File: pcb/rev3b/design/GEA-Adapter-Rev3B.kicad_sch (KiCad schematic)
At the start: 100 parts, among them J1 8P8C, J2 RECOVERY, J3 TC2030, Q3 CJ3407, Q4 CJ3407, Q5 MMBT3904, U10 TPS22810DBVR, U2 XIAO ESP32-C3 v1.3 (22-pad), U4 74LVC2G07, U5 74LVC2G07_3v3, U8 AP63205WU, U9 TPS22810DBVR

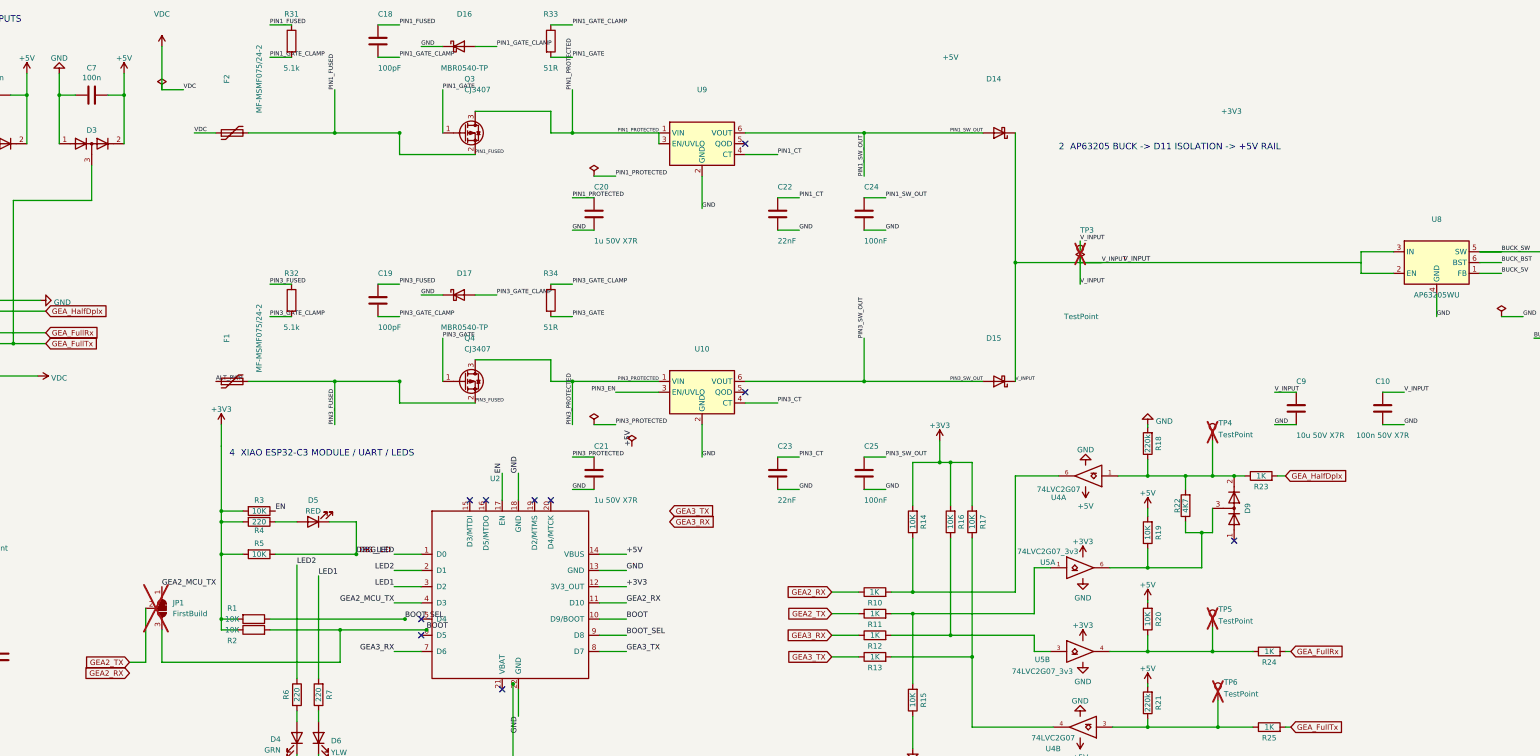
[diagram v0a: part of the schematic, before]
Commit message: fix(pcb): resolve Rev3B schematic warnings and label spacing
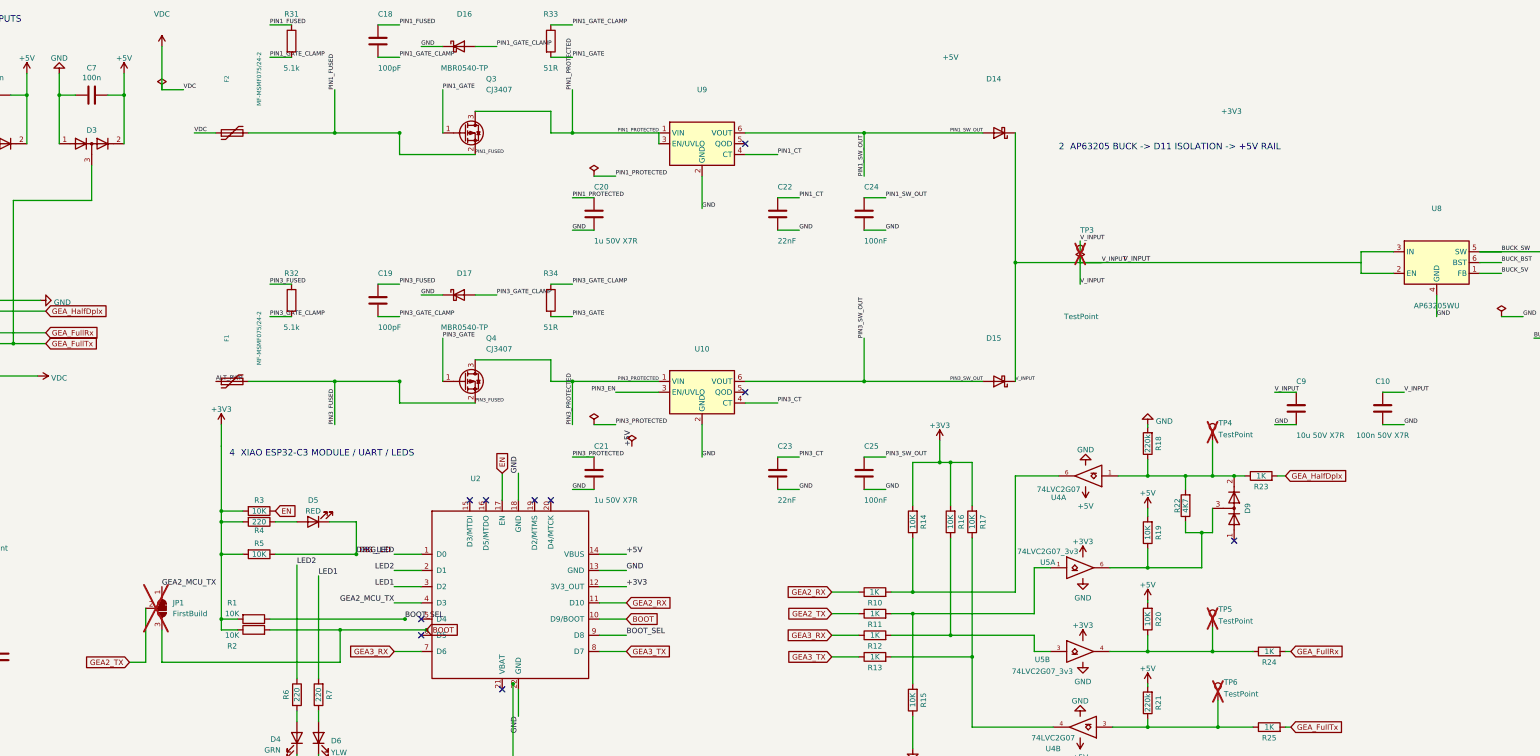
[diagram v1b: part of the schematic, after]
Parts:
- U4: symbol 74xGxx:74LVC2G07 -> GEA_Rev3B:74LVC2G07
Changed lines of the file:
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@@
 		)
 	)
-	(global_label "GEA3_TX"
-		(shape input)
-		(at 223.52 134.62 0)
-		(fields_autoplaced yes)
-		(effects
-			(font
-				(size 1.27 1.27)
-			)
-			(justify left)
-		)
-		(property "Intersheetrefs" "${INTERSHEET_REFS}"
-			(at 233.7128 134.62 0)
-			(effects
-				(font
-					(size 1.27 1.27)
-				)
-				(justify left)
-				(hide yes)
-			)
-		)
-	)
 	(global_label "GEA3_RX"
 		(shape input)
@@
 		)
 	)
-	(global_label "GEA3_RX"
-		(shape input)
-		(at 223.52 137.16 0)
-		(fields_autoplaced yes)
-		(effects
-			(font
-				(size 1.27 1.27)
-			)
-			(justify left)
-		)
-		(property "Intersheetrefs" "${INTERSHEET_REFS}"
-			(at 234.0152 137.16 0)
-			(effects
-				(font
-					(size 1.27 1.27)
-				)
-				(justify left)
-				(hide yes)
-			)
-		)
-	)
-	(global_label "GEA2_RX"
-		(shape input)
-		(at 96.52 172.72 180)
-		(fields_autoplaced yes)
-		(effects
-			(font
-				(size 1.27 1.27)
-			)
-			(justify right)
-		)
-		(property "Intersheetrefs" "${INTERSHEET_REFS}"
-			(at 86.0248 172.72 0)
-			(effects
-				(font
-					(size 1.27 1.27)
-				)
-				(justify right)
-				(hide yes)
-			)
-		)
-	)
 	(symbol
 		(lib_id "Connector:8P8C")
@@
 			(effects
 				(font
-					(size 1.27 1.27)
+					(size 1 1)
 				)
 			)
@@
 			(effects
 				(font
-					(size 1.27 1.27)
+					(size 1 1)
 				)
 			)
@@
 		(dnp no)
 		(property "Reference" "R2"
-			(at 120.65 165.1 90)
+			(at 120.65 166.37 90)
 			(effects
 				(font
@@
 		)
 		(property "Value" "10K"
-			(at 120.65 162.56 90)
+			(at 120.65 163.83 90)
 			(effects
 				(font
@@
 		(dnp no)
 		(property "Reference" "R1"
-			(at 120.65 157.48 90)
+			(at 120.65 156.21 90)
 			(effects
 				(font
@@
 		)
 		(property "Value" "10K"
-			(at 120.65 160.02 90)
+			(at 120.65 158.75 90)
 			(effects
 				(font
@@
 	)
 	(symbol
-		(lib_id "74xGxx:74LVC2G07")
+		(lib_id "GEA_Rev3B:74LVC2G07")
 		(at 321.31 126.365 180)
 		(unit 1)
@@
 			(effects
 				(font
-					(size 1.27 1.27)
+					(size 1 1)
 				)
 			)
@@
 			(effects
 				(font
-					(size 1.27 1.27)
+					(size 1 1)
 				)
 			)
@@
 	)
 	(symbol
-		(lib_id "74xGxx:74LVC2G07")
+		(lib_id "GEA_Rev3B:74LVC2G07")
 		(at 320.04 185.42 180)
 		(unit 2)
@@
 		(dnp no)
 		(property "Reference" "U2"
-			(at 183.6735 127 0)
+			(at 179.07 127 0)
 			(effects
 				(font
@@
 		(dnp no)
 		(property "Reference" "U8"
-			(at 403.86 66.04 0)
+			(at 403.86 63.5 0)
 			(show_name no)
 			(do_not_autoplace no)
@@
 		)
 		(property "Value" "AP63205WU"
-			(at 403.86 83.82 0)
+			(at 403.86 86.36 0)
 			(show_name no)
 			(do_not_autoplace no)
@@
 		(dnp no)
 		(property "Reference" "Q3"
-			(at 175.26 33.02 0)
+			(at 180.34 33.02 0)
 			(show_name no)
 			(do_not_autoplace no)
@@
 		)
 		(property "Value" "CJ3407"
-			(at 175.26 35.56 0)
+			(at 180.34 35.56 0)
 			(show_name no)
 			(do_not_autoplace no)
@@
 		(dnp no)
 		(property "Reference" "Q4"
-			(at 175.26 93.98 0)
+			(at 180.34 93.98 0)
 			(show_name no)
 			(do_not_autoplace no)
@@
 		)
 		(property "Value" "CJ3407"
-			(at 175.26 96.52 0)
+			(at 180.34 96.52 0)
 			(show_name no)
 			(do_not_autoplace no)
@@
 		)
 	)
-	(label "BOOT"
+	(global_label "BOOT"
+		(shape input)
 		(at 166.37 162.56 0)
-		(effects (font (size 1.27 1.27)) (justify left bottom))
+		(fields_autoplaced yes)
+		(effects (font (size 1.27 1.27)) (justify left))
+		(property "Intersheetrefs" "${INTERSHEET_REFS}"
+			(at 176.5348 162.56 0)
+			(effects (font (size 1.27 1.27)) (justify left) (hide yes))
+		)
 	)
 	(text "XIAO ESP32-C3 (22-pad OPL symbol). Native USB stays on the module.\nPad 14 VUSB is tied directly to +5V; pad 21 VBAT is unused."
@@
 	(label "LED1" (at 158.75 152.4 180) (effects (font (size 1.27 1.27)) (justify right bottom)))
 	(label "GEA2_MCU_TX" (at 158.75 156.21 180) (effects (font (size 1.27 1.27)) (justify right bottom)))
-	(label "GEA3_RX" (at 158.75 167.64 180) (effects (font (size 1.27 1.27)) (justify right bottom)))
-	(label "GEA3_TX" (at 213.36 167.64 0) (effects (font (size 1.27 1.27)) (justify left bottom)))
+	(global_label "GEA3_RX" (shape input) (at 158.75 167.64 180) (fields_autoplaced yes) (effects (font (size 1.27 1.27)) (justify right))
+		(property "Intersheetrefs" "${INTERSHEET_REFS}" (at 148.5752 167.64 0) (effects (font (size 1.27 1.27)) (justify right) (hide yes)))
+	)
+	(global_label "GEA3_TX" (shape input) (at 213.36 167.64 0) (fields_autoplaced yes) (effects (font (size 1.27 1.27)) (justify left))
+		(property "Intersheetrefs" "${INTERSHEET_REFS}" (at 223.5348 167.64 0) (effects (font (size 1.27 1.27)) (justify left) (hide yes)))
+	)
 	(label "BOOT_SEL" (at 213.36 163.83 0) (effects (font (size 1.27 1.27)) (justify left bottom)))
-	(label "BOOT" (at 213.36 160.02 0) (effects (font (size 1.27 1.27)) (justify left bottom)))
-	(label "GEA2_RX" (at 213.36 156.21 0) (effects (font (size 1.27 1.27)) (justify left bottom)))
+	(global_label "BOOT" (shape input) (at 213.36 160.02 0) (fields_autoplaced yes) (effects (font (size 1.27 1.27)) (justify left))
+		(property "Intersheetrefs" "${INTERSHEET_REFS}" (at 223.5348 160.02 0) (effects (font (size 1.27 1.27)) (justify left) (hide yes)))
+	)
+	(global_label "GEA2_RX" (shape input) (at 213.36 156.21 0) (fields_autoplaced yes) (effects (font (size 1.27 1.27)) (justify left))
+		(property "Intersheetrefs" "${INTERSHEET_REFS}" (at 223.5348 156.21 0) (effects (font (size 1.27 1.27)) (justify left) (hide yes)))
+	)
 	(label "+3V3" (at 213.36 152.4 0) (effects (font (size 1.27 1.27)) (justify left bottom)))
 	(label "GND" (at 213.36 148.59 0) (effects (font (size 1.27 1.27)) (justify left bottom)))
 	(label "+5V" (at 213.36 144.78 0) (effects (font (size 1.27 1.27)) (justify left bottom)))
-	(label "EN" (at 184.15 125.73 90) (effects (font (size 1.27 1.27)) (justify left bottom)))
+	(global_label "EN" (shape input) (at 184.15 125.73 90) (fields_autoplaced yes) (effects (font (size 1.27 1.27)) (justify left))
+		(property "Intersheetrefs" "${INTERSHEET_REFS}" (at 184.15 115.5552 0) (effects (font (size 1.27 1.27)) (justify left) (hide yes)))
+	)
 	(label "GND" (at 187.96 125.73 90) (effects (font (size 1.27 1.27)) (justify left bottom)))
 	(no_connect
@@
 	(global_label "EN" (shape input) (at 36.83 227.33 180) (effects (font (size 1.27 1.27)) (justify right)))
 	(global_label "BOOT" (shape input) (at 36.83 240.03 180) (effects (font (size 1.27 1.27)) (justify right)))
-	(label "EN" (at 130.81 134.62 0) (effects (font (size 1.27 1.27)) (justify left bottom)))
+	(global_label "EN" (shape input) (at 130.81 134.62 0) (fields_autoplaced yes) (effects (font (size 1.27 1.27)) (justify left))
+		(property "Intersheetrefs" "${INTERSHEET_REFS}" (at 140.9848 134.62 0) (effects (font (size 1.27 1.27)) (justify left) (hide yes)))
+	)
 	(label "ALT_PWR" (at 64.135 97.79 180) (effects (font (size 1.27 1.27)) (justify right bottom)))
 	(label "5V_IN" (at 44.45 207.01 180) (effects (font (size 1.27 1.27)) (justify right bottom)))
